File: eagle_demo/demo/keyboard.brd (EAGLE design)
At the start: 50 x 50 mm, 9 parts, among them X1 CLAMP_1X2-T-2.5MM, X2 CLAMP_1X2-T-2.5MM

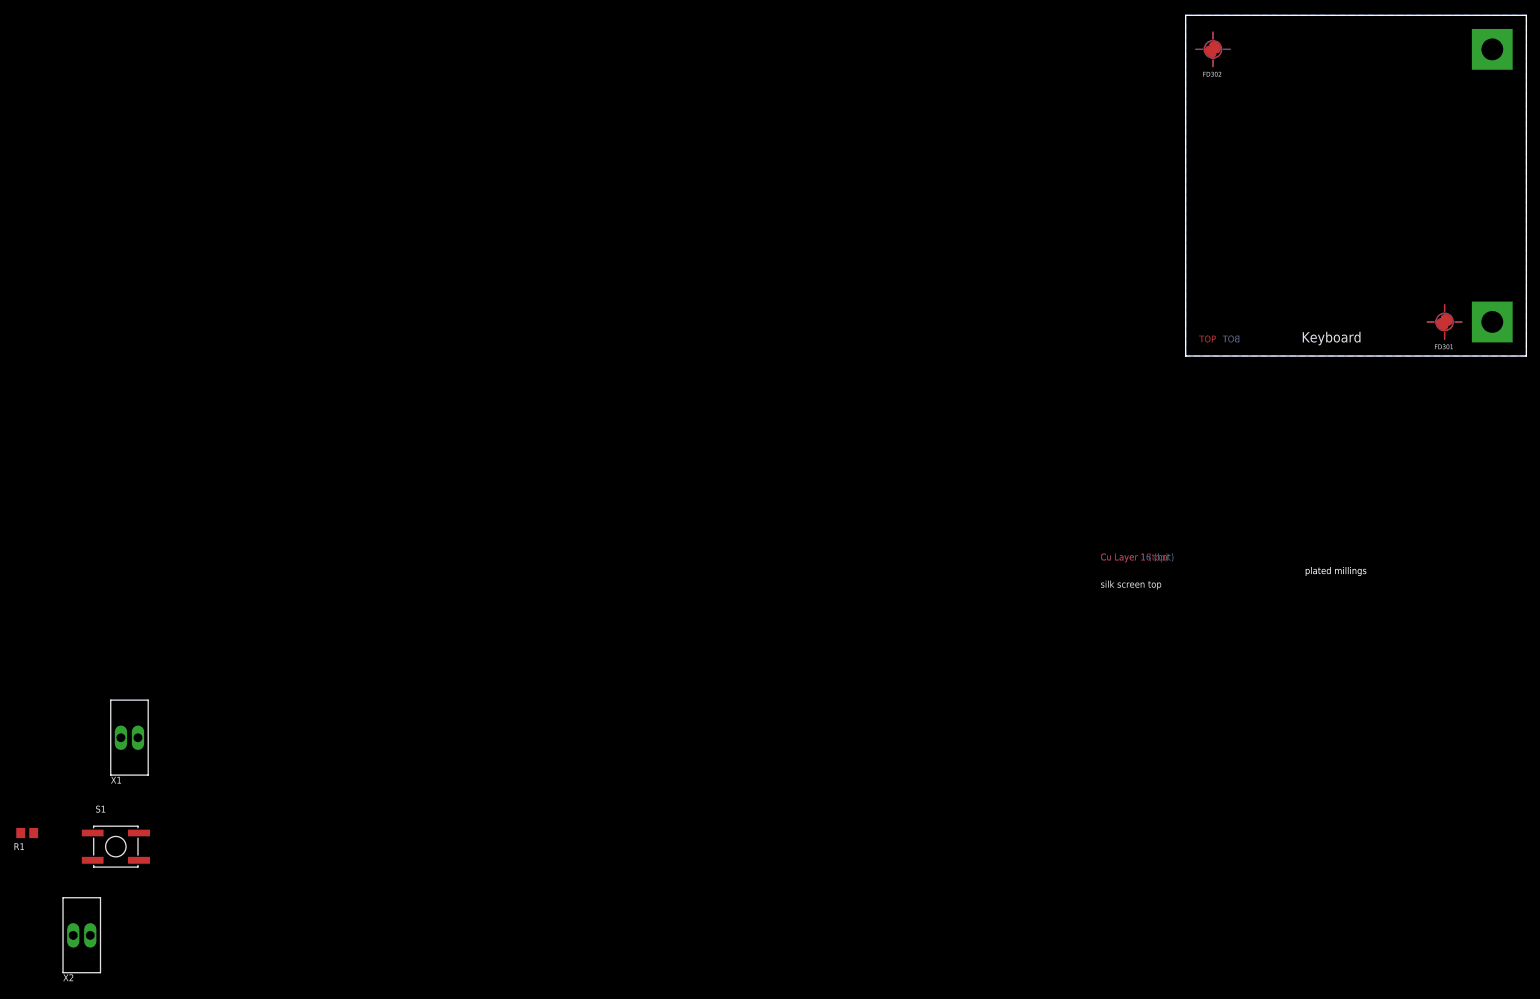
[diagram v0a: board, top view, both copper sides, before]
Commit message: step 1.4 keyboard layout
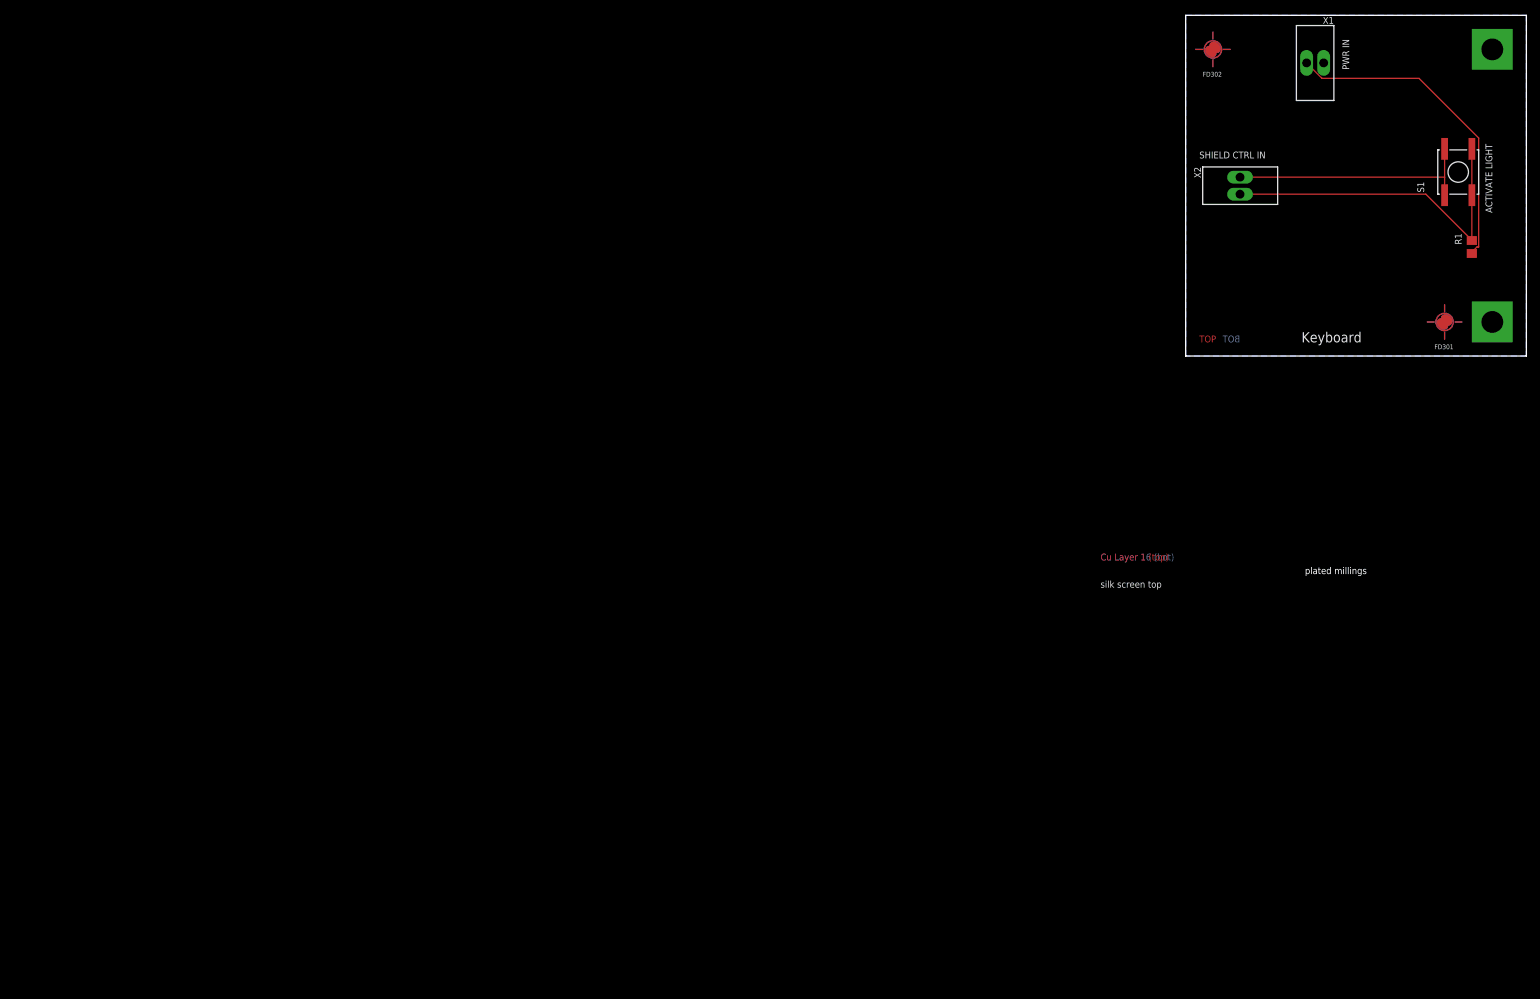
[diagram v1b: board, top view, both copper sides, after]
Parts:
- moved R1 228.8 mm to (42.0, 16.0), turned to 270 degrees
- moved S1 220.5 mm to (40.0, 27.0), turned to 90 degrees
- moved X2 202.5 mm to (8.00, 25.0), turned to 270 degrees
- moved X1 200.2 mm to (19.0, 43.0), turned to 180 degrees
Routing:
- net KBD_OUT: track 0.00 -> 50.3 mm
- net P5V: track 0.00 -> 47.3 mm
- net GND: track 0.00 -> 36.8 mm
